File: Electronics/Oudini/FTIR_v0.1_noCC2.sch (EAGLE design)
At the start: 104 parts, among them CON1 SPI, IC1 REG1117, Q1 IRF3704S, Q3 IRF3704S, Q4 BSP75, Q7 IRF3704S, Q8 BSP75, X3 16MHz, X4 MINI-USB

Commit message: main board Oudini on the way, 2.5V ref generator missing for the DAC stage, guard ring to be added on C1 C2 (see datasheet DAC1220)
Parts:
- removed 3.3V-OK: RED, adafruit:LEDCHIPLED_1206
- removed C4: 100nF, rcl:C-EUC1206
- removed C5: 10uF, rcl:C-EUC1206
- removed C6: 220nF, rcl:C-EUC1206
- removed D5: 1N581D1206, lpatiny:1N581D1206
- removed IC1: REG1117, burr-brown:REG1117
- removed R16, R18: 10k, rcl:R-EU_R0805
- removed R17: 1k, rcl:R-EU_R0805
- removed R27: 1K, rcl:R-EU_R0805
- added 5V-FAN: (no value), con-lstb:MA03-1
- added U$20: STARGND, lpatiny:STARGND
- C1: value 10uF -> 100nF
- R32: value 1k -> 14.3k
- U$1: value SST25VF064C -> M24512; device BertaLib:SST25VF064C -> lpatiny:M24512
- U$5: value CHIPCAP -> STARGND; device lpatiny:CHIPCAP -> lpatiny:STARGND
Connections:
- removed net 3.3V: C1.1, C6.1, IC1.VOUT, R1.2, R16.2, R27.2, U$1.HOLD, U$1.VCC, U$1.WP, U$5.VDD
- removed net DGND: C13.1, C14.1, U$15.VSS
- removed net FMOSI: D5.A, R1.1, U$1.MOSI
- removed net N$10: R16.1, R17.1, U$1.CS
- removed net N$20: 3.3V-OK.A, R27.1
- removed net N$23: R18.2, U$1.SCK
- removed net N$8: C4.1, U$5.VCORE
- net +5V: now also 5V-FAN.2; no longer C13.2, C14.2, C18.2, PIEZO.5, R10.1, R12.2, R14.2, R2.1, R21.1, R28.1, R29.1, R39.2, R4.2, R9.1, SENSOR.5, U$10.VCC, U$11.VCC, U$12.VCC, U$13.VCC, U$14.AVDD, U$14.DVDD, U$15.VDD, U$9.VCC
- net +5V/1: now also C1.1, C13.2, C14.2, C18.2, PIEZO.5, R10.1, R12.2, R14.2, R2.1, R21.1, R28.1, R29.1, R39.2, R4.2, R9.1, SENSOR.5, U$1.VCC, U$10.VCC, U$11.VCC, U$12.VCC, U$13.VCC, U$14.AVDD, U$14.DVDD, U$15.VDD, U$9.VCC; no longer C5.1, IC1.VIN
- net A4: now also R1.2
- net AGND: now also R1.1, U$20.AGND, U$5.AGND; no longer U$4.GND2, U$4.GND3
- net CS: no longer R17.2
- net D11*: now also U$1.-WC
- net GND: now also 5V-FAN.1, C13.1, C14.1, U$1.E0, U$1.E1, U$1.E2, U$1.VSS, U$15.VSS, U$20.DGND, U$20.GND, U$4.GND2, U$4.GND3, U$5.DGND; no longer 3.3V-OK.C, C4.2, C5.2, C6.2, IC1.GND, U$1.GND
- net MISO: no longer U$1.MISO
- net MOSI: no longer D5.C
- net SCK: no longer R18.1
- net SCL: now also U$1.SCL; no longer U$5.SCL
- net SDA: now also U$1.SDA; no longer U$5.SDA
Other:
- note added: "I2C EEPROM 1M"
- note added: "Peltier 5V fan"
- note removed: "CC2"
- note removed: "Flash Memory"
- moved on the sheet: C1, R1, R10, R2, R21, R9, RL6, RL7, RL8, RL9, U$1

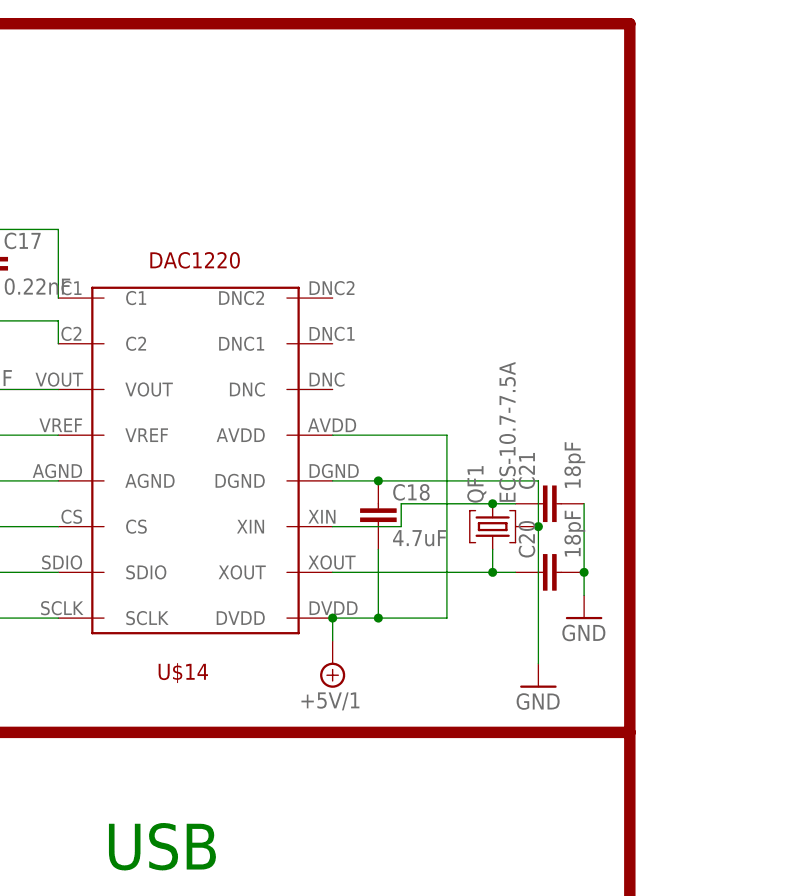
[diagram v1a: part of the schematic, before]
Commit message: finalisation of main FTIR board (Oudini)
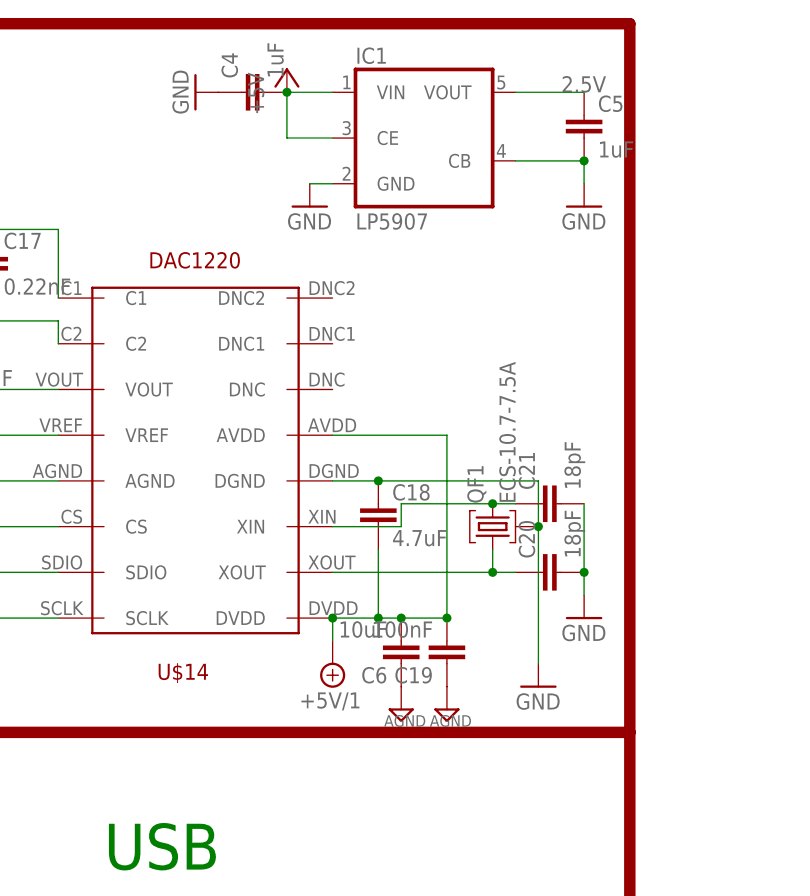
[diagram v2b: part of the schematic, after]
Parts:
- added C19: 100nF, rcl:C-EUC1206
- added C4, C5: 1uF, rcl:C-EUC1206
- added C6: 10uF, rcl:C-EUC1206
- added IC1: LP5907, v-reg:TS520525
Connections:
- net +5V: now also C4.2, IC1.CE, IC1.VIN
- net +5V/1: now also C19.2, C6.2
- net 2.5V: now also C5.1, IC1.VOUT
- net AGND: now also C19.1, C6.1
- net GND: now also C4.1, C5.2, IC1.CB, IC1.GND
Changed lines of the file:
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@@
 <part name="GND9" library="supply1" deviceset="GND" device=""/>
 <part name="P+1" library="supply1" deviceset="+5V" device=""/>
+<part name="IC1" library="v-reg" deviceset="TS5205" device="" technology="25" value="LP5907"/>
+<part name="GND32" library="supply1" deviceset="GND" device=""/>
+<part name="C5" library="rcl" deviceset="C-EU" device="C1206" value="1uF"/>
+<part name="GND33" library="supply1" deviceset="GND" device=""/>
+<part name="C4" library="rcl" deviceset="C-EU" device="C1206" value="1uF"/>
+<part name="GND34" library="supply1" deviceset="GND" device=""/>
+<part name="P+3" library="supply1" deviceset="+5V" device=""/>
+<part name="C6" library="rcl" deviceset="C-EU" device="C1206" value="10uF"/>
+<part name="C19" library="rcl" deviceset="C-EU" device="C1206" value="100nF"/>
+<part name="AGND2" library="supply2" deviceset="AGND" device="" value="AGND"/>
+<part name="AGND10" library="supply2" deviceset="AGND" device="" value="AGND"/>
 </parts>
 <sheets>
@@
 </instance>
 <instance part="P+1" gate="1" x="-20.32" y="238.76" rot="R180"/>
+<instance part="IC1" gate="G$1" x="271.78" y="332.74"/>
+<instance part="GND32" gate="1" x="259.08" y="325.12"/>
+<instance part="C5" gate="G$1" x="289.56" y="335.28"/>
+<instance part="GND33" gate="1" x="289.56" y="325.12"/>
+<instance part="C4" gate="G$1" x="251.46" y="337.82" rot="R90"/>
+<instance part="GND34" gate="1" x="246.38" y="337.82" rot="R270"/>
+<instance part="P+3" gate="1" x="256.54" y="340.36"/>
+<instance part="C6" gate="G$1" x="269.24" y="274.32" rot="R180"/>
+<instance part="C19" gate="G$1" x="274.32" y="274.32" smashed="yes" rot="R180">
+<attribute name="NAME" x="272.796" y="273.939" size="1.778" layer="95" rot="R180"/>
+<attribute name="VALUE" x="272.796" y="279.019" size="1.778" layer="96" rot="R180"/>
+</instance>
+<instance part="AGND2" gate="G$1" x="269.24" y="269.24" smashed="yes">
+<attribute name="VALUE" x="267.335" y="267.335" size="1.27" layer="96"/>
+</instance>
+<instance part="AGND10" gate="G$1" x="274.32" y="269.24" smashed="yes">
+<attribute name="VALUE" x="272.415" y="267.335" size="1.27" layer="96"/>
+</instance>
 </instances>
 <busses>
@@
 <wire x1="-2.54" y1="241.3" x2="-20.32" y2="241.3" width="0.1524" layer="91"/>
 <pinref part="P+1" gate="1" pin="+5V"/>
+</segment>
+<segment>
+<pinref part="IC1" gate="G$1" pin="VIN"/>
+<wire x1="261.62" y1="337.82" x2="256.54" y2="337.82" width="0.1524" layer="91"/>
+<junction x="256.54" y="337.82"/>
+<pinref part="C4" gate="G$1" pin="2"/>
+<wire x1="256.54" y1="337.82" x2="256.54" y2="332.74" width="0.1524" layer="91"/>
+<pinref part="IC1" gate="G$1" pin="CE"/>
+<wire x1="256.54" y1="332.74" x2="261.62" y2="332.74" width="0.1524" layer="91"/>
+<pinref part="P+3" gate="1" pin="+5V"/>
 </segment>
 </net>
@@
 <wire x1="81.28" y1="284.48" x2="86.36" y2="284.48" width="0.1524" layer="91"/>
 <pinref part="GND9" gate="1" pin="GND"/>
+</segment>
+<segment>
+<pinref part="C5" gate="G$1" pin="2"/>
+<pinref part="GND33" gate="1" pin="GND"/>
+<wire x1="289.56" y1="330.2" x2="289.56" y2="327.66" width="0.1524" layer="91"/>
+<pinref part="IC1" gate="G$1" pin="CB"/>
+<wire x1="281.94" y1="330.2" x2="289.56" y2="330.2" width="0.1524" layer="91"/>
+<junction x="289.56" y="330.2"/>
+</segment>
+<segment>
+<pinref part="C4" gate="G$1" pin="1"/>
+<pinref part="GND34" gate="1" pin="GND"/>
+</segment>
+<segment>
+<pinref part="IC1" gate="G$1" pin="GND"/>
+<pinref part="GND32" gate="1" pin="GND"/>
+<wire x1="259.08" y1="327.66" x2="261.62" y2="327.66" width="0.1524" layer="91"/>
 </segment>
 </net>
@@
 <wire x1="266.7" y1="279.4" x2="266.7" y2="287.02" width="0.1524" layer="91"/>
 <junction x="261.62" y="279.4"/>
-<wire x1="266.7" y1="279.4" x2="274.32" y2="279.4" width="0.1524" layer="91"/>
+<wire x1="266.7" y1="279.4" x2="269.24" y2="279.4" width="0.1524" layer="91"/>
+<wire x1="269.24" y1="279.4" x2="274.32" y2="279.4" width="0.1524" layer="91"/>
 <wire x1="274.32" y1="279.4" x2="274.32" y2="299.72" width="0.1524" layer="91"/>
 <junction x="266.7" y="279.4"/>
@@
 <wire x1="274.32" y1="299.72" x2="261.62" y2="299.72" width="0.1524" layer="91"/>
 <pinref part="SUPPLY2" gate="G$1" pin="+5V/1"/>
+<pinref part="C6" gate="G$1" pin="2"/>
+<junction x="269.24" y="279.4"/>
+<pinref part="C19" gate="G$1" pin="2"/>
+<junction x="274.32" y="279.4"/>
 </segment>
 <segment>
@@
 <wire x1="106.68" y1="279.4" x2="101.6" y2="279.4" width="0.1524" layer="91"/>
 </segment>
+<segment>
+<pinref part="C6" gate="G$1" pin="1"/>
+<pinref part="AGND2" gate="G$1" pin="AGND"/>
+</segment>
+<segment>
+<pinref part="C19" gate="G$1" pin="1"/>
+<pinref part="AGND10" gate="G$1" pin="AGND"/>
+</segment>
 </net>
 <net name="N$14" class="3">
@@
 <label x="213.36" y="299.72" size="1.778" layer="95"/>
 </segment>
-</net>
+<segment>
+<pinref part="IC1" gate="G$1" pin="VOUT"/>
+<pinref part="C5" gate="G$1" pin="1"/>
+<wire x1="281.94" y1="337.82" x2="289.56" y2="337.82" width="0.1524" layer="91"/>
+<label x="287.02" y="337.82" size="1.778" layer="95"/>
+</segment>
+</net>

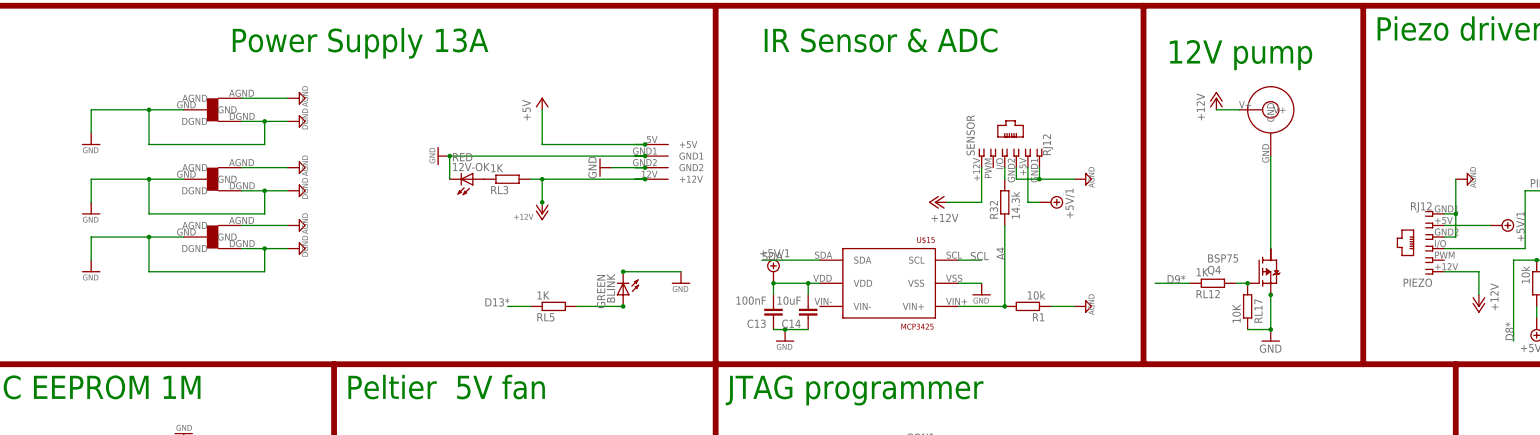
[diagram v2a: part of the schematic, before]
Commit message: finished sensor board for D205B, finished main board Oudini v1.0, Generated Gerbers, modified CAD for PCB support
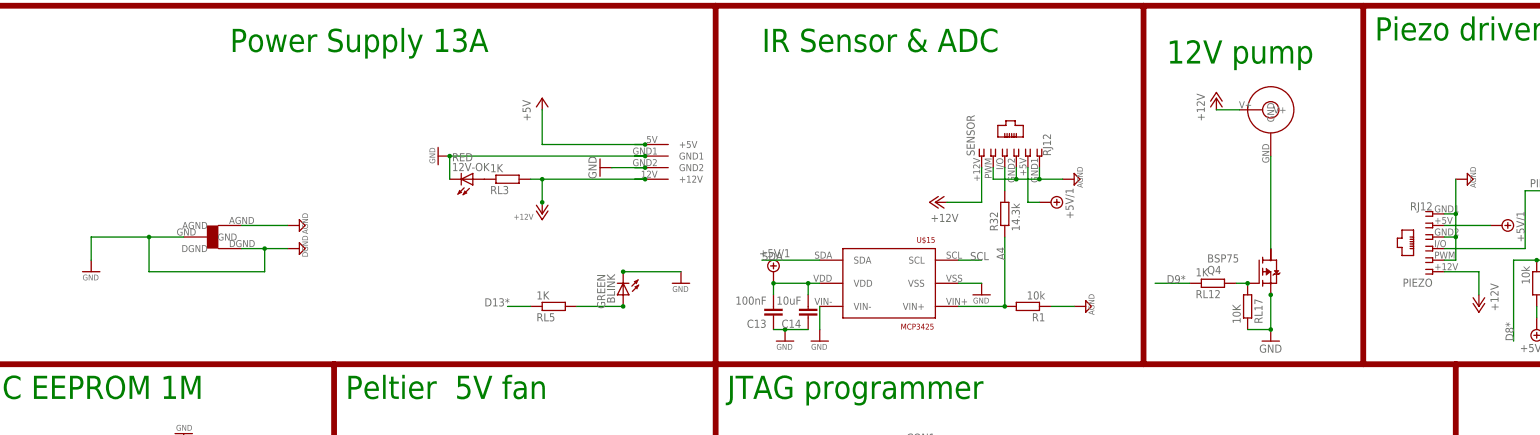
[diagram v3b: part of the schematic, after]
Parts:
- removed U$2, U$20: STARGND, lpatiny:STARGND
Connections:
- net AGND: now also PIEZO.2, SENSOR.2; no longer U$2.AGND, U$20.AGND
- net GND: now also U$15.VIN-; no longer U$2.DGND, U$2.GND, U$20.DGND, U$20.GND
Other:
- moved on the sheet: R32
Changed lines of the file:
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@@
 </classes>
 <parts>
-<part name="GND19" library="supply1" deviceset="GND" device=""/>
 <part name="SENSOR" library="lpatiny" deviceset="RJ12" device="STRAIGHT" value="RJ12"/>
 <part name="R32" library="rcl" deviceset="R-EU_" device="R0805" value="14.3k"/>
@@
 <part name="RL6" library="rcl" deviceset="R-EU_" device="R0805" value="1K"/>
 <part name="RL8" library="rcl" deviceset="R-EU_" device="R0805" value="1K"/>
-<part name="U$2" library="lpatiny" deviceset="STARGND" device=""/>
-<part name="AGND" library="supply2" deviceset="AGND" device="" value="AGND"/>
-<part name="DGND" library="supply2" deviceset="DGND" device="" value="DGND"/>
 <part name="DGND1" library="supply2" deviceset="DGND" device="" value="DGND"/>
 <part name="DGND2" library="supply2" deviceset="DGND" device="" value="DGND"/>
@@
 <part name="AGND7" library="supply2" deviceset="AGND" device="" value="AGND"/>
 <part name="DGND10" library="supply2" deviceset="DGND" device="" value="DGND"/>
-<part name="GND15" library="supply1" deviceset="GND" device=""/>
-<part name="U$20" library="lpatiny" deviceset="STARGND" device=""/>
-<part name="AGND8" library="supply2" deviceset="AGND" device="" value="AGND"/>
-<part name="DGND14" library="supply2" deviceset="DGND" device="" value="DGND"/>
 <part name="R1" library="rcl" deviceset="R-EU_" device="R0805" value="10k"/>
 <part name="AGND9" library="supply2" deviceset="AGND" device="" value="AGND"/>
@@
 <part name="AGND2" library="supply2" deviceset="AGND" device="" value="AGND"/>
 <part name="AGND10" library="supply2" deviceset="AGND" device="" value="AGND"/>
+<part name="GND15" library="supply1" deviceset="GND" device=""/>
 </parts>
 <sheets>
@@
 </plain>
 <instances>
-<instance part="GND19" gate="1" x="-109.22" y="299.72" smashed="yes">
-<attribute name="VALUE" x="-111.125" y="297.815" size="1.27" layer="96"/>
-</instance>
 <instance part="SENSOR" gate="G$1" x="91.44" y="312.42" rot="R90"/>
-<instance part="R32" gate="G$1" x="91.44" y="302.26" rot="R90"/>
+<instance part="R32" gate="G$1" x="91.44" y="299.72" rot="R90"/>
 <instance part="P+12" gate="1" x="76.2" y="302.26" rot="R90"/>
 <instance part="PIEZO" gate="G$1" x="185.42" y="292.1" rot="R180"/>
@@
 <instance part="RL6" gate="G$1" x="-25.4" y="182.88" rot="MR180"/>
 <instance part="RL8" gate="G$1" x="-25.4" y="162.56" rot="MR180"/>
-<instance part="U$2" gate="G$1" x="-83.82" y="307.34"/>
-<instance part="AGND" gate="G$1" x="-63.5" y="309.88" smashed="yes" rot="R90">
-<attribute name="VALUE" x="-61.595" y="307.975" size="1.27" layer="96" rot="R90"/>
-</instance>
-<instance part="DGND" gate="G$1" x="-63.5" y="304.8" smashed="yes" rot="R90">
-<attribute name="VALUE" x="-61.595" y="302.895" size="1.27" layer="96" rot="R90"/>
-</instance>
 <instance part="DGND1" gate="G$1" x="-5.08" y="177.8" smashed="yes">
 <attribute name="VALUE" x="-6.985" y="175.895" size="1.27" layer="96"/>
@@
 <attribute name="VALUE" x="194.945" y="305.435" size="1.27" layer="96" rot="R90"/>
 </instance>
-<instance part="AGND5" gate="G$1" x="109.22" y="307.34" smashed="yes" rot="R90">
-<attribute name="VALUE" x="111.125" y="305.435" size="1.27" layer="96" rot="R90"/>
+<instance part="AGND5" gate="G$1" x="106.68" y="307.34" smashed="yes" rot="R90">
+<attribute name="VALUE" x="108.585" y="305.435" size="1.27" layer="96" rot="R90"/>
 </instance>
 <instance part="U$1" gate="G$1" x="-104.14" y="226.06"/>
@@
 <attribute name="VALUE" x="-61.595" y="290.195" size="1.27" layer="96" rot="R90"/>
 </instance>
-<instance part="GND15" gate="1" x="-109.22" y="314.96" smashed="yes">
-<attribute name="VALUE" x="-111.125" y="313.055" size="1.27" layer="96"/>
-</instance>
-<instance part="U$20" gate="G$1" x="-83.82" y="322.58"/>
-<instance part="AGND8" gate="G$1" x="-63.5" y="325.12" smashed="yes" rot="R90">
-<attribute name="VALUE" x="-61.595" y="323.215" size="1.27" layer="96" rot="R90"/>
-</instance>
-<instance part="DGND14" gate="G$1" x="-63.5" y="320.04" smashed="yes" rot="R90">
-<attribute name="VALUE" x="-61.595" y="318.135" size="1.27" layer="96" rot="R90"/>
-</instance>
 <instance part="R1" gate="G$1" x="96.52" y="279.4" rot="R180"/>
 <instance part="AGND9" gate="G$1" x="109.22" y="279.4" smashed="yes" rot="R90">
@@
 <attribute name="VALUE" x="272.415" y="267.335" size="1.27" layer="96"/>
 </instance>
+<instance part="GND15" gate="1" x="50.8" y="271.78" smashed="yes">
+<attribute name="VALUE" x="48.895" y="269.875" size="1.27" layer="96"/>
+</instance>
 </instances>
 <busses>
@@
 </net>
 <net name="GND" class="1">
-<segment>
-<wire x1="-109.22" y1="307.34" x2="-109.22" y2="302.26" width="0.1524" layer="91"/>
-<pinref part="GND19" gate="1" pin="GND"/>
-<pinref part="U$2" gate="G$1" pin="GND"/>
-<wire x1="-88.9" y1="307.34" x2="-96.52" y2="307.34" width="0.1524" layer="91"/>
-<wire x1="-96.52" y1="307.34" x2="-109.22" y2="307.34" width="0.1524" layer="91"/>
-<wire x1="-96.52" y1="307.34" x2="-96.52" y2="299.72" width="0.1524" layer="91"/>
-<pinref part="U$2" gate="G$1" pin="DGND"/>
-<wire x1="-76.2" y1="304.8" x2="-71.12" y2="304.8" width="0.1524" layer="91"/>
-<pinref part="DGND" gate="G$1" pin="DGND"/>
-<wire x1="-71.12" y1="304.8" x2="-66.04" y2="304.8" width="0.1524" layer="91"/>
-<wire x1="-96.52" y1="299.72" x2="-71.12" y2="299.72" width="0.1524" layer="91"/>
-<wire x1="-71.12" y1="299.72" x2="-71.12" y2="304.8" width="0.1524" layer="91"/>
-<junction x="-96.52" y="307.34"/>
-<junction x="-71.12" y="304.8"/>
-</segment>
 <segment>
 <pinref part="X4" gate="G$1" pin="5"/>
@@
 </segment>
 <segment>
-<wire x1="-109.22" y1="322.58" x2="-109.22" y2="317.5" width="0.1524" layer="91"/>
-<pinref part="GND15" gate="1" pin="GND"/>
-<pinref part="U$20" gate="G$1" pin="GND"/>
-<wire x1="-88.9" y1="322.58" x2="-96.52" y2="322.58" width="0.1524" layer="91"/>
-<wire x1="-96.52" y1="322.58" x2="-109.22" y2="322.58" width="0.1524" layer="91"/>
-<wire x1="-96.52" y1="322.58" x2="-96.52" y2="314.96" width="0.1524" layer="91"/>
-<pinref part="U$20" gate="G$1" pin="DGND"/>
-<wire x1="-76.2" y1="320.04" x2="-71.12" y2="320.04" width="0.1524" layer="91"/>
-<pinref part="DGND14" gate="G$1" pin="DGND"/>
-<wire x1="-71.12" y1="320.04" x2="-66.04" y2="320.04" width="0.1524" layer="91"/>
-<wire x1="-96.52" y1="314.96" x2="-71.12" y2="314.96" width="0.1524" layer="91"/>
-<wire x1="-71.12" y1="314.96" x2="-71.12" y2="320.04" width="0.1524" layer="91"/>
-<junction x="-96.52" y="322.58"/>
-<junction x="-71.12" y="320.04"/>
-</segment>
-<segment>
 <pinref part="C1" gate="G$1" pin="2"/>
 <wire x1="-88.9" y1="246.38" x2="-88.9" y2="248.92" width="0.1524" layer="91"/>
@@
 <pinref part="GND32" gate="1" pin="GND"/>
 <wire x1="259.08" y1="327.66" x2="261.62" y2="327.66" width="0.1524" layer="91"/>
+</segment>
+<segment>
+<pinref part="U$15" gate="G$1" pin="VIN-"/>
+<pinref part="GND15" gate="1" pin="GND"/>
+<wire x1="50.8" y1="279.4" x2="50.8" y2="274.32" width="0.1524" layer="91"/>
 </segment>
 </net>
@@
 <pinref part="U$15" gate="G$1" pin="VIN+"/>
 <wire x1="81.28" y1="279.4" x2="91.44" y2="279.4" width="0.1524" layer="91"/>
-<wire x1="91.44" y1="279.4" x2="91.44" y2="297.18" width="0.1524" layer="91"/>
+<wire x1="91.44" y1="279.4" x2="91.44" y2="294.64" width="0.1524" layer="91"/>
 <pinref part="R1" gate="G$1" pin="2"/>
 <junction x="91.44" y="279.4"/>
@@
 <pinref part="R32" gate="G$1" pin="2"/>
 <pinref part="SENSOR" gate="G$1" pin="3"/>
-<wire x1="91.44" y1="307.34" x2="91.44" y2="309.88" width="0.1524" layer="91"/>
+<wire x1="91.44" y1="304.8" x2="91.44" y2="309.88" width="0.1524" layer="91"/>
 </segment>
 </net>
@@
 <net name="AGND" class="0">
 <segment>
-<pinref part="U$2" gate="G$1" pin="AGND"/>
-<wire x1="-76.2" y1="309.88" x2="-66.04" y2="309.88" width="0.1524" layer="91"/>
-<pinref part="AGND" gate="G$1" pin="AGND"/>
-</segment>
-<segment>
 <pinref part="C11" gate="G$1" pin="2"/>
 <wire x1="35.56" y1="119.38" x2="35.56" y2="109.22" width="0.1524" layer="91"/>
@@
 <wire x1="190.5" y1="299.72" x2="190.5" y2="307.34" width="0.1524" layer="91"/>
 <pinref part="AGND4" gate="G$1" pin="AGND"/>
+<pinref part="PIEZO" gate="G$1" pin="2"/>
+<wire x1="187.96" y1="289.56" x2="190.5" y2="289.56" width="0.1524" layer="91"/>
+<wire x1="190.5" y1="289.56" x2="190.5" y2="294.64" width="0.1524" layer="91"/>
+<junction x="190.5" y="294.64"/>
 </segment>
 <segment>
@@
 <wire x1="93.98" y1="307.34" x2="99.06" y2="307.34" width="0.1524" layer="91"/>
 <junction x="99.06" y="307.34"/>
-<wire x1="99.06" y1="307.34" x2="106.68" y2="307.34" width="0.1524" layer="91"/>
+<wire x1="99.06" y1="307.34" x2="104.14" y2="307.34" width="0.1524" layer="91"/>
 <pinref part="AGND5" gate="G$1" pin="AGND"/>
+<pinref part="SENSOR" gate="G$1" pin="2"/>
+<wire x1="93.98" y1="307.34" x2="88.9" y2="307.34" width="0.1524" layer="91"/>
+<wire x1="88.9" y1="307.34" x2="88.9" y2="309.88" width="0.1524" layer="91"/>
+<junction x="93.98" y="307.34"/>
 </segment>
 <segment>
@@
 <wire x1="-76.2" y1="297.18" x2="-66.04" y2="297.18" width="0.1524" layer="91"/>
 <pinref part="AGND7" gate="G$1" pin="AGND"/>
-</segment>
-<segment>
-<pinref part="U$20" gate="G$1" pin="AGND"/>
-<wire x1="-76.2" y1="325.12" x2="-66.04" y2="325.12" width="0.1524" layer="91"/>
-<pinref part="AGND8" gate="G$1" pin="AGND"/>
 </segment>
 <segment>
@@
 </sheet>
 </sheets>
+<errors>
+</errors>
 </schematic>
 </drawing>
